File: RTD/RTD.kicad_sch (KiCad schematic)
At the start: 4 parts, among them J1 Screw_Terminal_01x04, J2 Screw_Terminal_01x04, U1 RP2040

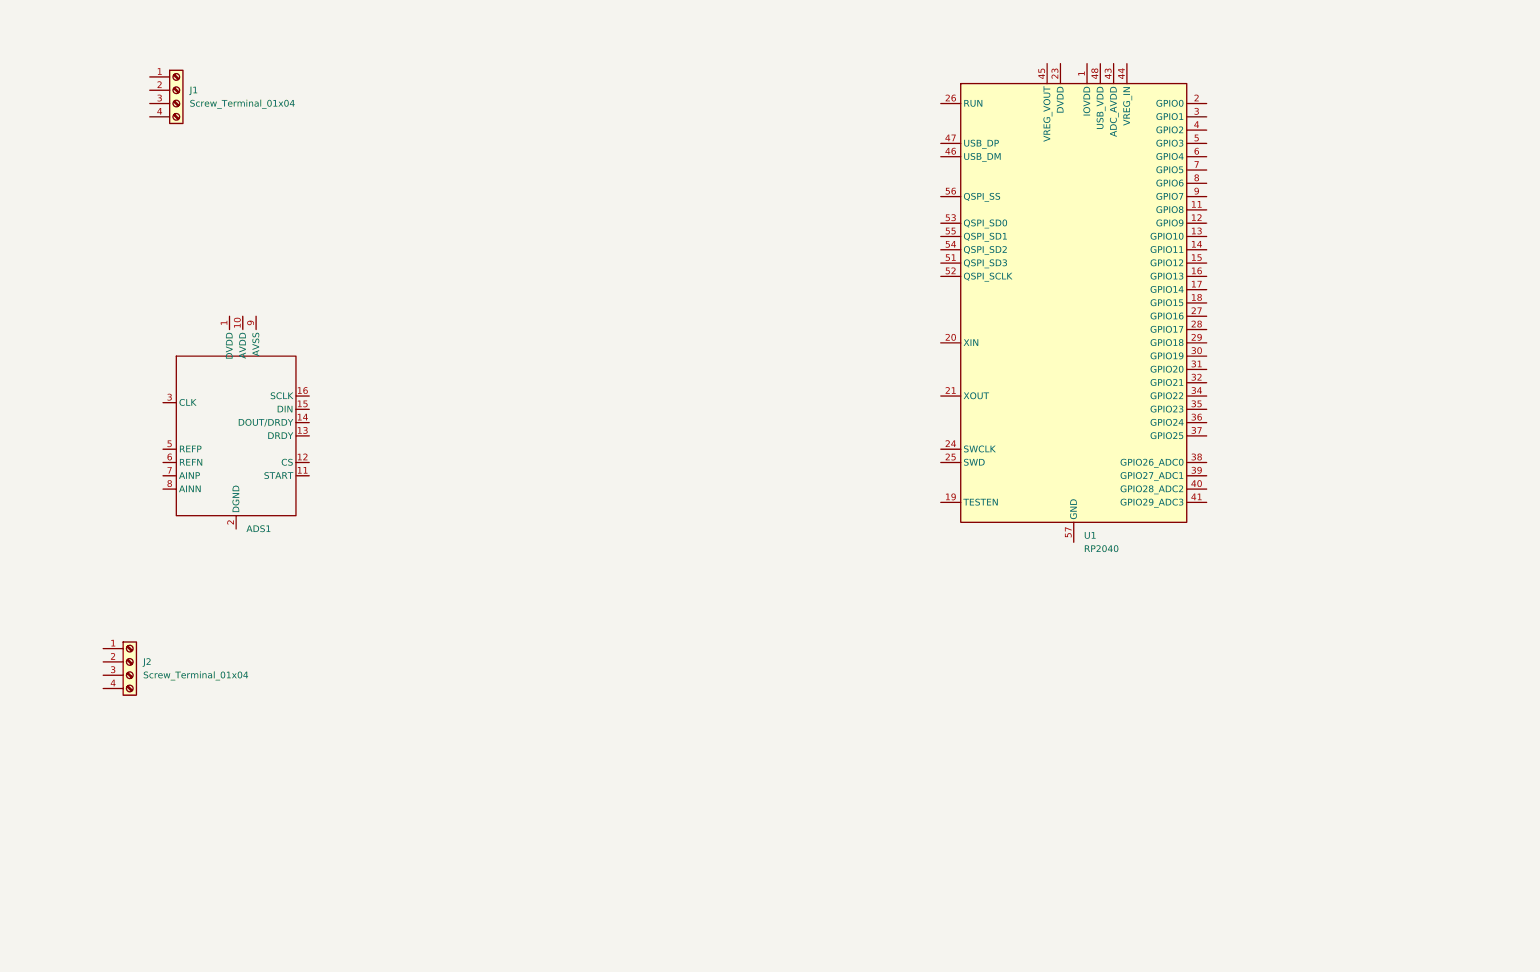
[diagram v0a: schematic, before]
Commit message: feat: adds ads1248
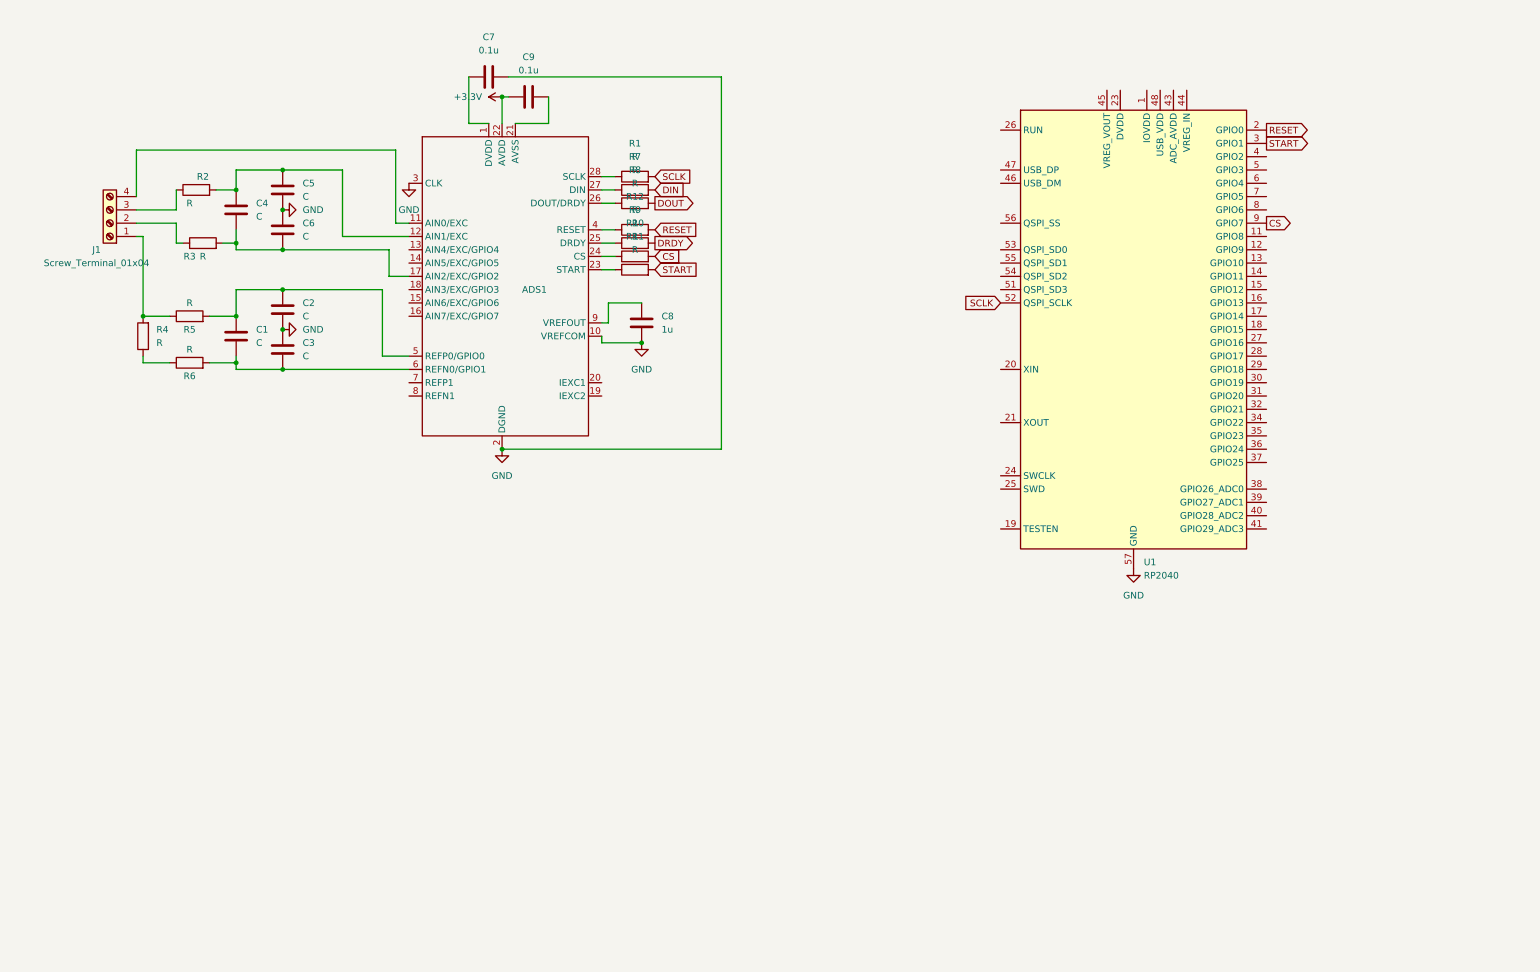
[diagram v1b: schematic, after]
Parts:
- removed J2: Screw_Terminal_01x04, symbol Connector:Screw_Terminal_01x04
- added C1, C2, C3, C4, C5, C6: C, symbol Device:C
- added C7, C9: 0.1u, symbol Device:C
- added C8: 1u, symbol Device:C
- added R1, R10, R11, R12, R2, R3, R4, R5, R6, R7, R8, R9: R, symbol Device:R
- ADS1: symbol ADC_SIGMA_DELTA_TI_ADS:ADS1246 -> ADC_SIGMA_DELTA_TI_ADS:ADS1248
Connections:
- net at ADS1.1 (DVDD): now also C7.1
- net GND: now reaches ADS1.10 (VREFCOM)
- net GND: now also ADS1.2 (DGND), ADS1.3 (CLK), U1.57 (GND), C2.2, C3.1, C5.2, C6.1, C7.2, C8.2
- net at ADS1.11 (AIN0/EXC): now also J1.4 (Pin_4)
- net at ADS1.12 (AIN1/EXC): now also C4.1, C5.1, R2.2
- net at ADS1.5 (REFP0/GPIO0): now also C1.1, C2.1, R5.2
- net at ADS1.6 (REFN0/GPIO1): now also C1.2, C3.2, R6.2
- net at ADS1.9 (VREFOUT): now also C8.1
- net RESET: now reaches U1.2 (GPIO0)
- net RESET: now also R12.2
- net START: now reaches U1.3 (GPIO1)
- net START: now also R11.2
- net SCLK: now reaches U1.52 (QSPI_SCLK)
- net SCLK: now also R1.2
- net CS: now reaches U1.9 (GPIO7)
- net CS: now also R10.2
- net at J1.1 (Pin_1): now also R4.2, R5.1
- net at J1.2 (Pin_2): now also R3.1
- net at J1.3 (Pin_3): now also R2.1
- new net: ADS1.17 (AIN2/EXC/GPIO2), C4.2, C6.2, R3.2
- new net: ADS1.26 (DOUT/DRDY), R8.1
- new net: ADS1.24 (CS), R10.1
- new net: ADS1.25 (DRDY), R9.1
- new net: ADS1.21 (AVSS), C9.2
- new net: ADS1.23 (START), R11.1
- new net: ADS1.27 (DIN), R7.1
- new net: ADS1.28 (SCLK), R1.1
- new net: ADS1.4 (RESET), R12.1
- new net: R4.1, R6.1
- new net +3.3V: ADS1.22 (AVDD), C9.1
- new net DIN: R7.2
- new net DOUT: R8.2
- new net DRDY: R9.2
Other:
- moved on the sheet: J1, U1

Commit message: version one of design is complete
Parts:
- removed U1: RP2040, Package_DFN_QFN:QFN-56-1EP_7x7mm_P0.4mm_EP3.2x3.2mm, symbol MCU_RaspberryPi:RP2040
- added C1, C2: 10u, symbol Device:C
- added C12, C19: 10n, symbol Device:C
- added C13, C14, C15, C16, C17, C18: 100n, symbol Device:C
- added C20: 1u, symbol Device:C
- added C21: C, symbol Device:C
- added F1: Polyfuse, symbol Device:Polyfuse
- added FB1: 120R, symbol Device:FerriteBead
- added J1: Conn_01x06_Pin, symbol Connector:Conn_01x06_Pin
- added L1, L2: 0.1mH, symbol Device:L
- added Pwr_term1: Screw_Terminal_01x02, symbol Connector:Screw_Terminal_01x02
- added R12: 10k, symbol Device:R
- added RS485_Term1: Screw_Terminal_01x03, symbol Connector:Screw_Terminal_01x03
- added SDT1: ~, symbol DC_DC_CONVERTER_XP_POWER_SDT:SDT01F24D3V3
- added SW1: SW_SPDT, symbol Switch:SW_SPDT
- added U1: THVD1420D, Package_SO:SOIC-8_3.9x4.9mm_P1.27mm, symbol Interface_UART:THVD1420D
- added U2: STM32F103C8Tx, Package_QFP:LQFP-48_7x7mm_P0.5mm, symbol MCU_ST_STM32F1:STM32F103C8Tx
- C3: renamed from C4; value C -> 0.047u
- C4: renamed from C1; value C -> 0.033u
- C5, C6: value C -> 4700p
- C7: renamed from C2; value C -> 3300p
- C8: renamed from C3; value C -> 3300p
- R1: renamed from R4; value R -> 1k
- R10, R11, R9: value R -> 47
- R2: renamed from R5; value R -> 5.49k
- R3: renamed from R2; value R -> 4.12k
- R4: renamed from R3; value R -> 4.12k
- R5: renamed from R1; value R -> 47
- R6: renamed from R7; value R -> 47
- R7: renamed from R8; value R -> 47
- R8: renamed from R12; value R -> 47
- renumbered R6 to 5.49k1, C9 to C10, C8 to C11, C7 to C9, J1 to PT_term1
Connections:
- net +3.3V: now also C12.2, C13.2, C14.2, C15.2, C16.2, C17.2, C18.2, C21.1, FB1.2, J1.1 (Pin_1), SDT1.4 (+VOUT), SW1.3 (C), U1.8 (VCC)
- net CS: now also U2.14 (PA4)
- net DIN: now also U2.17 (PA7)
- net DOUT: now also U2.16 (PA6)
- net DRDY: now also U2.3 (PC14)
- net GND: now also ADS1.21 (AVSS), C10.2, C9.1, C12.1, C13.1, C14.1, C15.1, C16.1, C17.1, C18.1, C19.2, C20.2, C21.2, J1.3 (Pin_3), Pwr_term1.1 (Pin_1), RS485_Term1.3 (Pin_3), SDT1.3 (-VOUT), SW1.1 (A), U1.5 (GND), U2.1 (VBAT), U2.23 (VSS), U2.24 (VDD), U2.35 (VSS), U2.36 (VDD), U2.47 (VSS), U2.48 (VDD), U2.8 (VSSA); no longer C9.2
- net RESET: now also U2.4 (PC15)
- net SCLK: now also U2.15 (PA5)
- net START: now also U2.2 (PC13)
- net at ADS1.1 (DVDD): now also C9.2; no longer C9.1
- new net: C1.1, F1.2, L2.1
- new net: C1.2, L1.1
- new net: RS485_Term1.1 (Pin_1), U1.7 (B)
- new net: RS485_Term1.2 (Pin_2), U1.6 (A)
- new net +24V: F1.1, Pwr_term1.2 (Pin_2)
- new net +3.3VA: C19.1, C20.1, FB1.1, U2.9 (VDDA)
- new net -24V: C2.2, L1.2, SDT1. (-VIN)
- new net 24V: C2.1, L2.2, SDT1. (-VIN)
- new net BOOT0: R12.1, U2.44 (BOOT0)
- new net DE: U1.3 (DE), U2.42 (PB6)
- new net NRST: J1.5 (Pin_5), U2.7 (NRST)
- new net RE: U1.2 (~{RE}), U2.41 (PB5)
- new net RX: U1.1 (RO), U2.13 (PA3)
- new net SWCLK: J1.2 (Pin_2), U2.37 (PA14)
- new net SWDIO: J1.4 (Pin_4), U2.34 (PA13)
- new net SWO: J1.6 (Pin_6), U2.39 (PB3)
- new net SW_BOOT0: R12.2, SW1.2 (B)
- new net TX: U1.4 (DI), U2.12 (PA2)
- no-connect marks 0 -> 32
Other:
- note added: "ADC AND LP FILTER"
- note added: "DC/DC converter: from 24V DIN Rail power supply to 3.3V"
- note added: "DEBUGGER"
- note added: "Decoupling capacitors"
- note added: "Designed with 1mA current"
- note added: "LP Filter for the RTD input: fc = 404.14Hz"
- note added: "LP filter for the reference. fc = 402.58Hz"
- note added: "MICROPROCESOR: STM32F103C8T"
- note added: "Note: all components can withstant above 101 degrees ambient temperature"
- note added: "POWER SUPPLY"
- note added: "RS485 TRANSCEIVER"
- note added: "VDDA filter"
- company: (none) -> BarbzBytes
- title: (none) -> Resistance Temperature Detector
- moved on the sheet: 5.49k1, ADS1, C10, C11, C3, C4, C5, C6, C7, C8, C9, PT_term1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

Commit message: feat: firmware project
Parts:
- removed J1: Conn_01x06_Pin, symbol Connector:Conn_01x06_Pin
- added Debug_power: Screw_Terminal_01x02, symbol Connector:Screw_Terminal_01x02
- added Debugger: Conn_01x05_Pin, symbol Connector:Conn_01x05_Pin
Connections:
- net +3.3V: now also Debug_power.2 (Pin_2), Debugger.1 (Pin_1)
- net GND: now also Debug_power.1 (Pin_1), Debugger.3 (Pin_3)
- net NRST: now also Debugger.5 (Pin_5)
- net SWCLK: now also Debugger.2 (Pin_2)
- net SWDIO: now also Debugger.4 (Pin_4)
- net SWO: no longer names the net of U2.39 (PB3)
- no-connect marks 32 -> 33
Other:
- note added: "Note: All components can withstand above 101 degrees ambient temperature"
- note added: "Power needs to be separate from the DIN Rail Input"
- note removed: "Note: all components can withstant above 101 degrees ambient temperature"
- moved on the sheet: C1, C2, F1, L1, L2, Pwr_term1, RS485_Term1, SDT1, U1

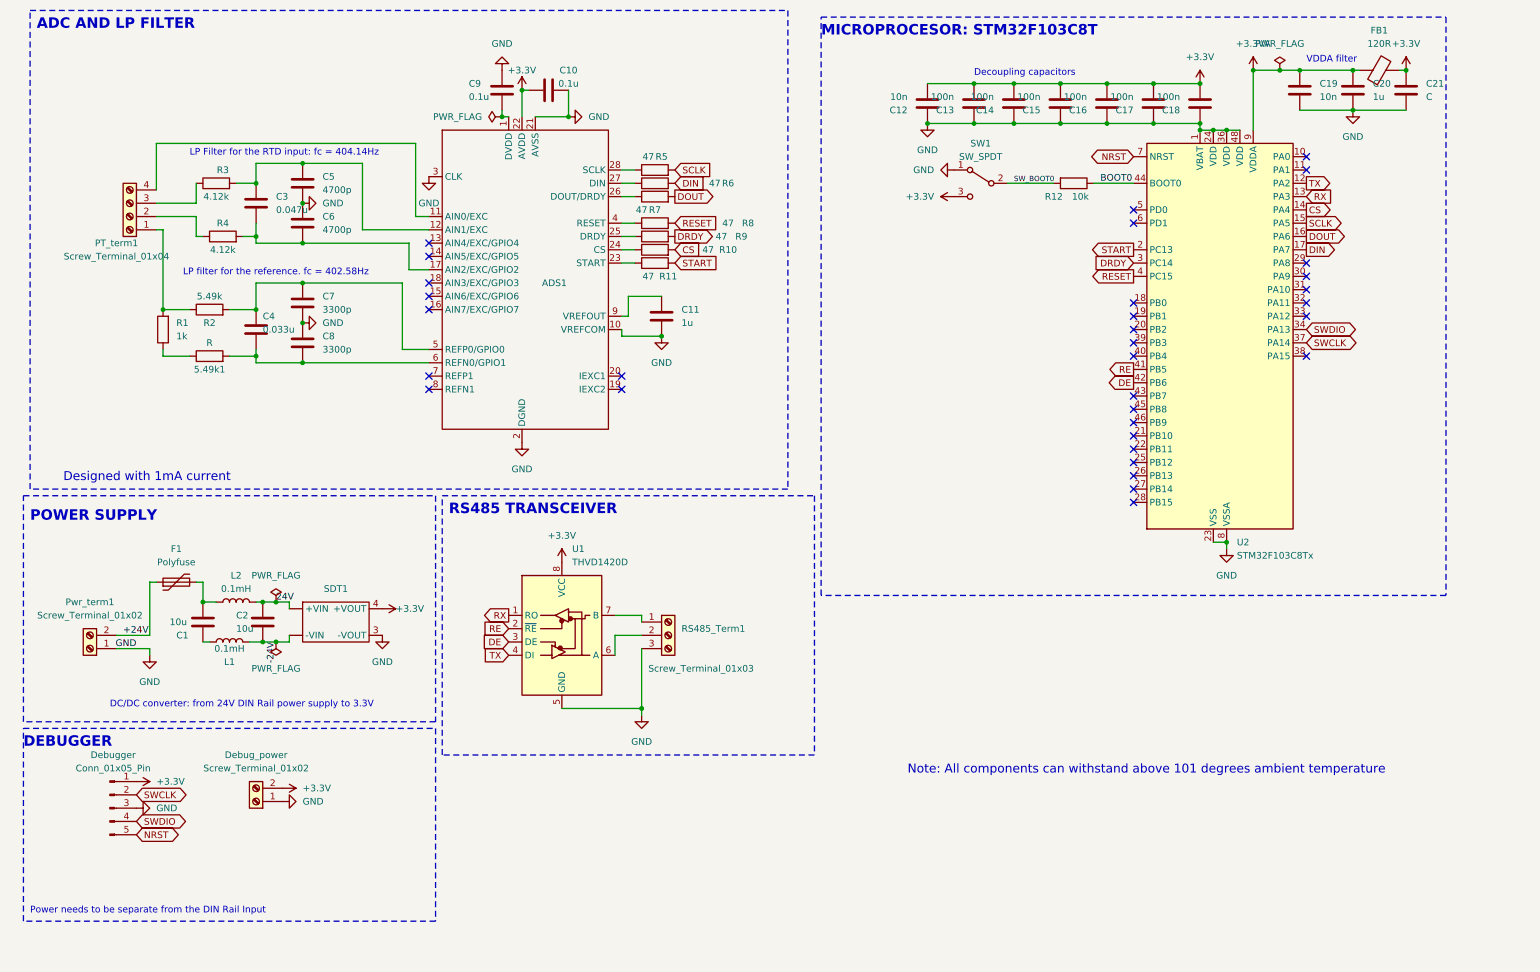
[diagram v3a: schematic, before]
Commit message: - feat: scffolded for firmware - refactor: edidted the schematics texts
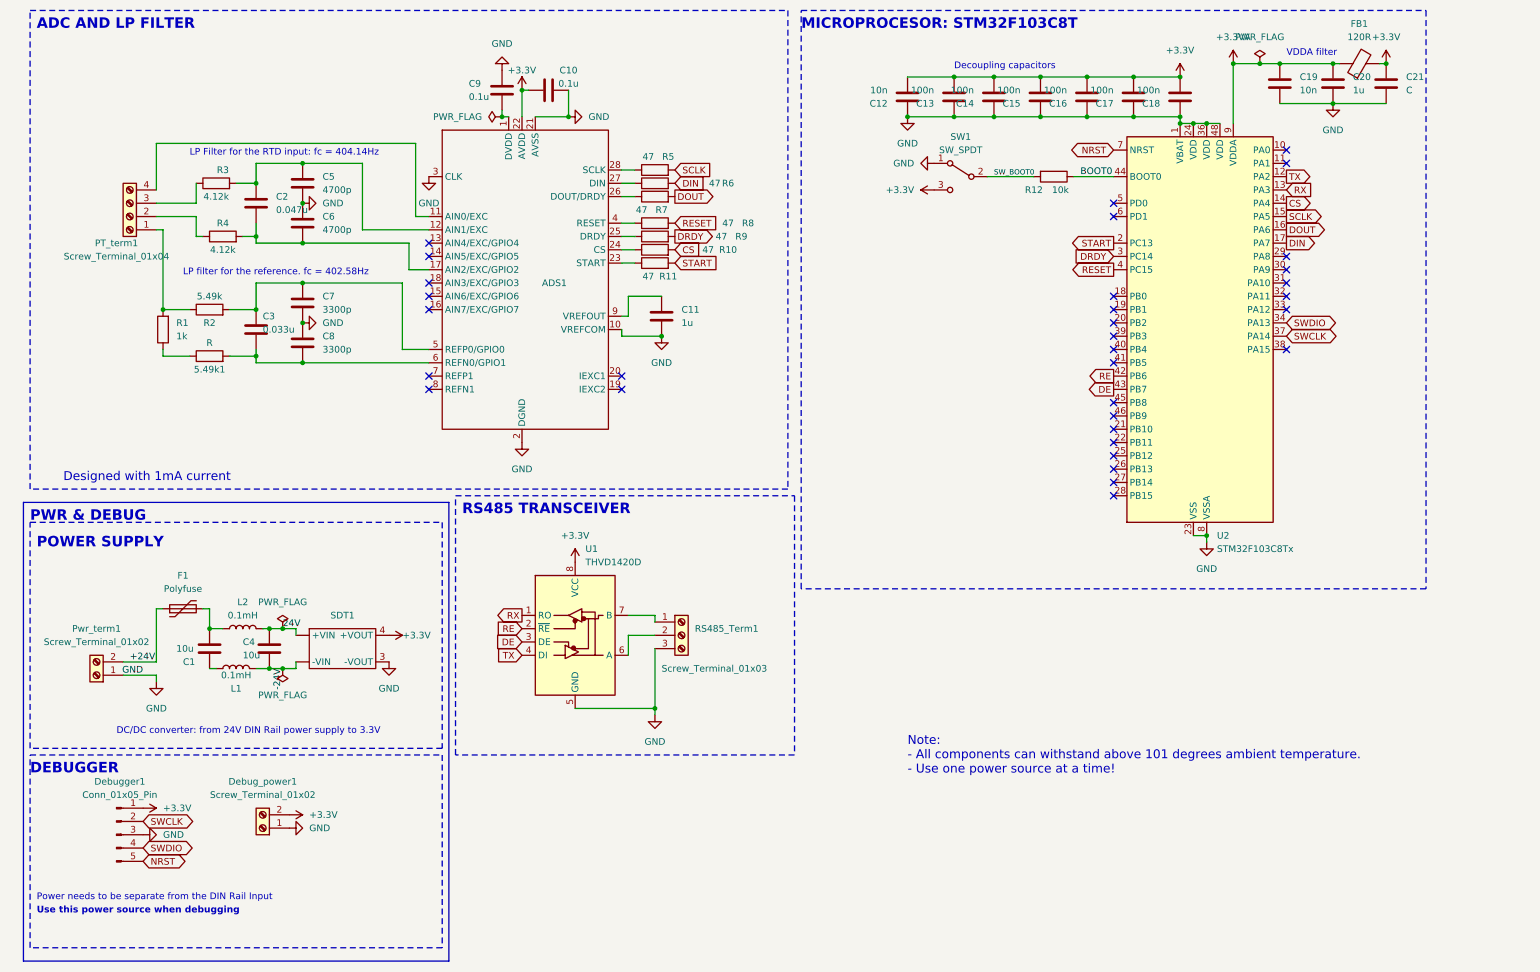
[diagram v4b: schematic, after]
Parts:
- renumbered C3 to C2, C4 to C3, C2 to C4, Debug_power to Debug_power1, Debugger to Debugger1
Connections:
- net DE: now also U2.43 (PB7); no longer U2.42 (PB6)
- net RE: now also U2.42 (PB6); no longer U2.41 (PB5)
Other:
- note added: "Note: - All components can withstand above 101 degrees ambient temperature. - Use one power source at a time!"
- note added: "PWR & DEBUG"
- note added: "Use this power source when debugging"
- note removed: "Note: All components can withstand above 101 degrees ambient temperature"
- moved on the sheet: C1, C12, C13, C14, C15, C16, C17, C18, C19, C20, C21, C4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
